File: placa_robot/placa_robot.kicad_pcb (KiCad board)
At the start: 2 copper layers, 75 x 80 mm, 34 parts, among them IC1 MSP430FR2355TPT, J1 Conn_01x03, J2 Conn_01x01, J3 Conn_02x04_Odd_Even, J4 conn_DFrobot, SW1 SW_Push, U1 LM324, Y1 Crystal

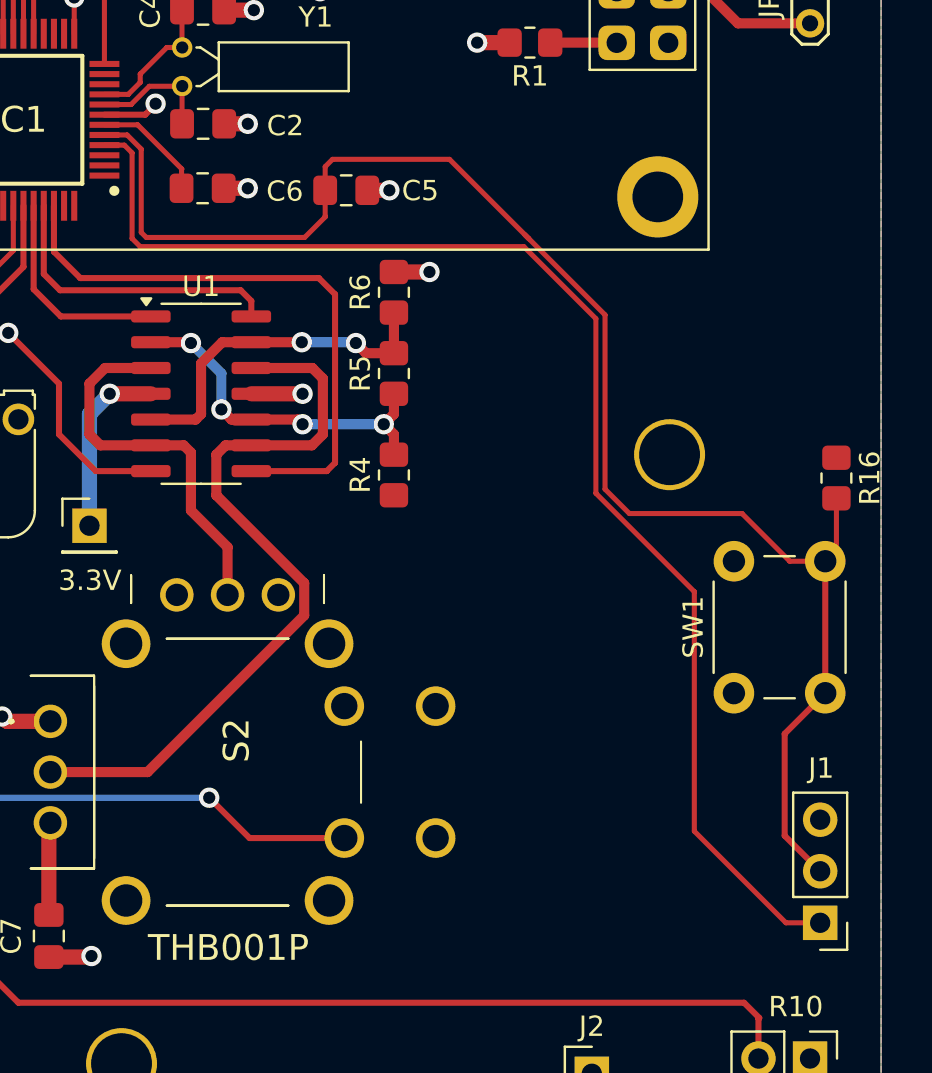
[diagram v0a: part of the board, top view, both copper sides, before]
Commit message: Modificar SBW layout
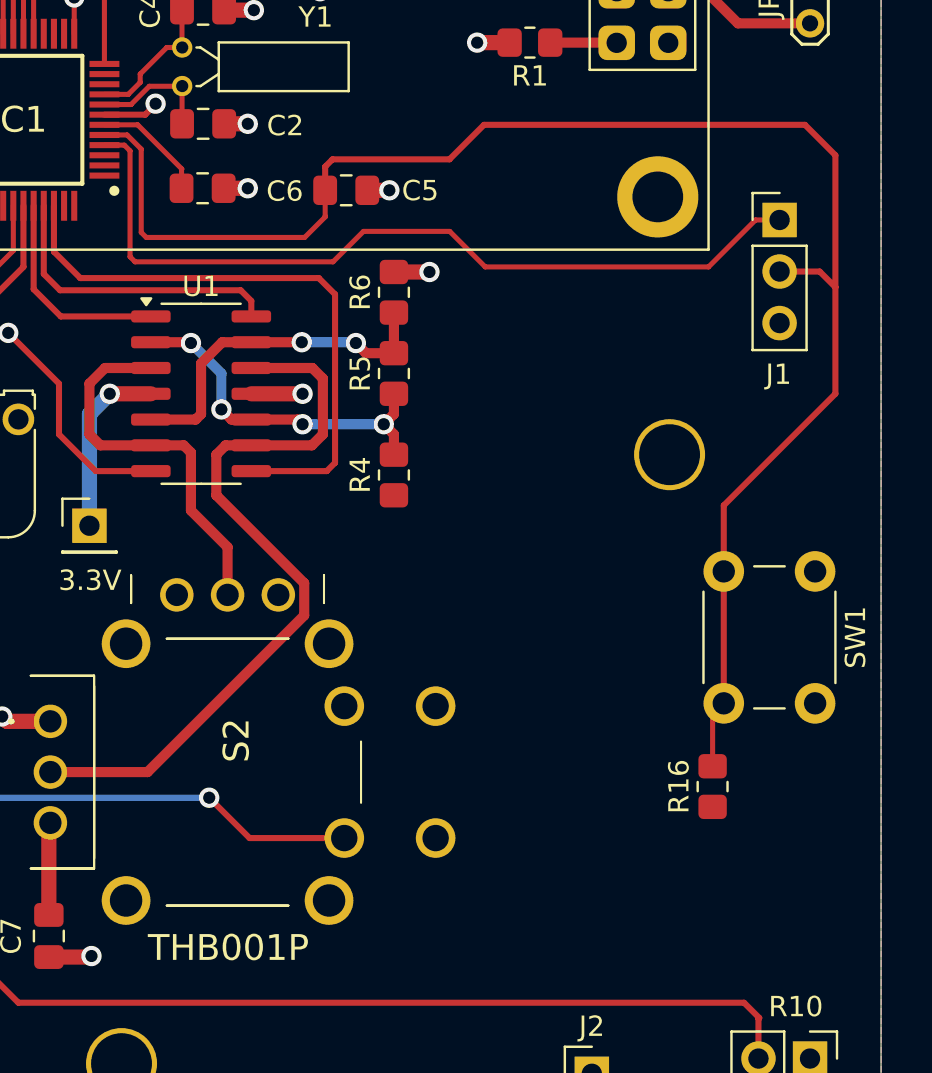
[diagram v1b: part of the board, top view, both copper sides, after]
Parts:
- moved J1 34.7 mm to (177.5, 75.9), turned to 0 degrees
- moved R16 16.4 mm to (174.2, 103.8), turned to 90 degrees
- moved SW1 7.21 mm to (179.2, 93.2), turned to -90 degrees
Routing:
- net /SBW: track 65.6 -> 41.0 mm
- net /MCU_RST: track 76.8 -> 80.6 mm
